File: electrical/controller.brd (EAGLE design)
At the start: 101.6 x 25.4 mm, 38 parts, among them IC1 555, Q1 IRLIB9343PBF-ND, Q3 600mA/40V, U1 POLOLU_D24V22F5, U3 MCP4725, U4 MCP4725, U5 MCP6142

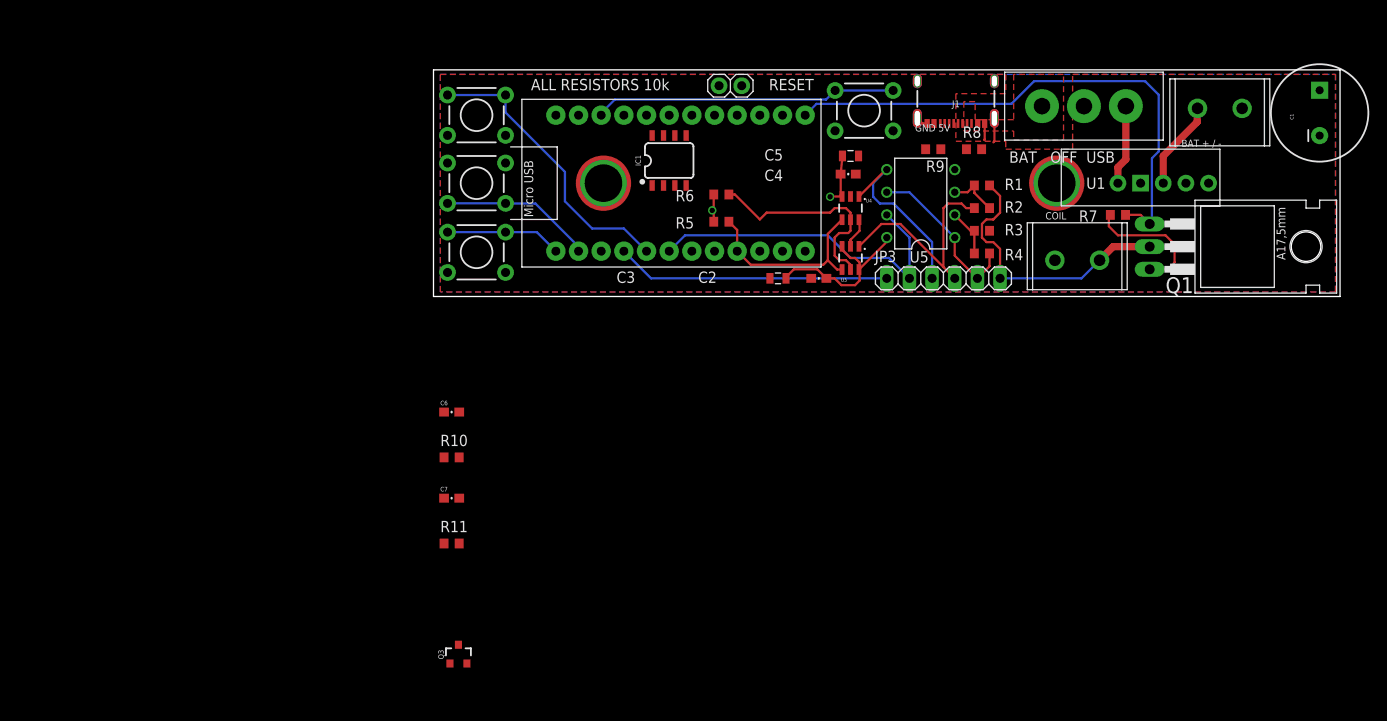
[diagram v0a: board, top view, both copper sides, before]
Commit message: Finish rev D1
Most of hte new features, except without overhauling the power system
b/c the power system requires tests with spools, which I havent done
yet.
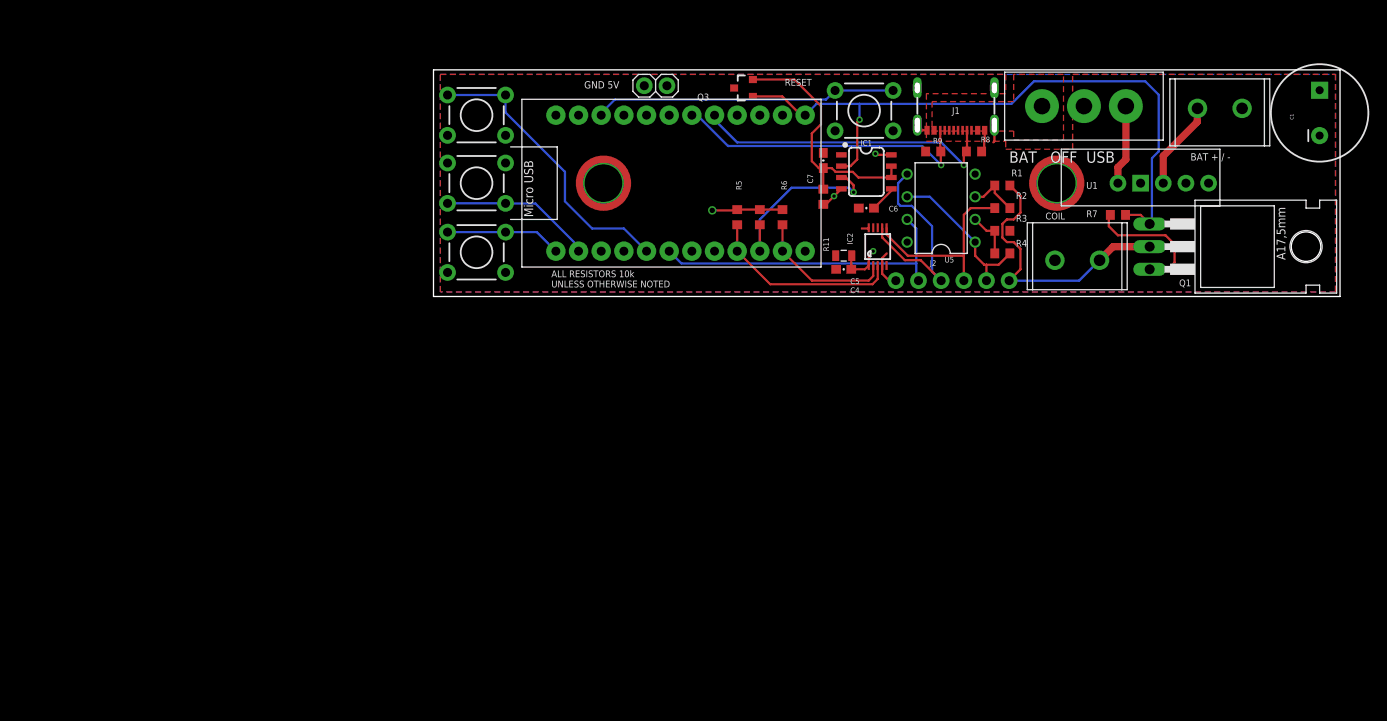
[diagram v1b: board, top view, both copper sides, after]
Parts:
- removed C2: .1uF, pie:0603-CAP
- removed C3: 10uF, pie:0805
- removed JP3: (no value), pinhead:1X06
- removed U3, U4: MCP4725, SparkFun-AnalogIC:SOT23-6
- added IC2: MCP4728, BEST_Custom:MSOP10
- added J2: (no value), SparkFun-Connectors:1X06_NO_SILK
- moved Q3 71.1 mm to (34.8, 23.4), turned to 90 degrees
- moved R11 57.0 mm to (43.7, 11.2), turned to 270 degrees
- moved C7 56.3 mm to (43.7, 15.2), turned to 270 degrees
- moved C6 51.8 mm to (48.5, 9.91), turned to 180 degrees
- moved R10 43.8 mm to (36.6, 8.89), turned to 270 degrees
- moved IC1 22.1 mm to (48.5, 14.0), turned to 270 degrees
- moved C5 11.2 mm to (46.0, 4.57), turned to 180 degrees
- moved C4 10.7 mm to (46.0, 3.05), turned to 180 degrees
- moved JP2 8.38 mm to (24.9, 23.6)
- moved R6 7.31 mm to (39.1, 8.89), turned to 90 degrees
- moved U5 2.34 mm to (56.9, 9.91)
- moved R1 2.29 mm to (63.8, 12.4)
- moved R2 2.29 mm to (63.8, 9.91)
- moved R3 2.29 mm to (63.8, 7.37)
- moved R4 2.29 mm to (63.8, 4.83)
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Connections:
- net 5V: now also IC2.1; no longer C2.1, C3.1, U3.3, U3.6, U4.3
- net COIL: now also J2.6; no longer JP3.6
- net GND: now also IC2.10, IC2.4, J2.1; no longer C2.2, C3.2, JP3.1, U3.2, U4.2, U4.6
- net INT: now also J2.2; no longer JP3.2
- net SCL: now also IC2.2; no longer U3.5, U4.5
- net SDA: now also IC2.3; no longer U3.4, U4.4
- net SHIFT: now also J2.5; no longer JP3.5
- net V1: now also IC2.6, J2.4; no longer JP3.4, U3.1
- net V2: now also IC2.7, J2.3; no longer JP3.3, U4.1
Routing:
- net CC1: track 0.00 -> 34.6 mm, vias 0 -> 1
- net CC2: track 0.00 -> 34.2 mm, vias 0 -> 1
- net GND: track 40.1 -> 11.0 mm
- net N$7: track 0.00 -> 28.8 mm
- net AUTO_RESTART: track 0.00 -> 21.2 mm, vias 0 -> 1
- net DRIVE: track 59.9 -> 75.0 mm, vias 0 -> 1
- net 5V: track 43.6 -> 32.7 mm, vias 2 -> 4
- net SCL: track 24.4 -> 15.9 mm
- net V2: track 20.8 -> 24.8 mm
- net V1: track 24.8 -> 21.5 mm
- net N$6: track 0.00 -> 2.97 mm
- net INT: track 37.8 -> 35.6 mm
- net SHIFT: track 18.7 -> 17.9 mm
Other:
- board text added: "ALL RESISTORS 10k UNLESS OTHERWISE NOTED"
- board text added: "Douglas Hutchings Double Pendulum Driver Rev D1"
- board text added: "NOTE: IF USING OSHPARK: In the DRC, set "elongation in the shapes tab To 150% This will ensure that the slots come out correctly!!"
- board text removed: "ALL RESISTORS 10k"
- board text removed: "Douglas Hutchings Double Pendulum Driver Rev C"

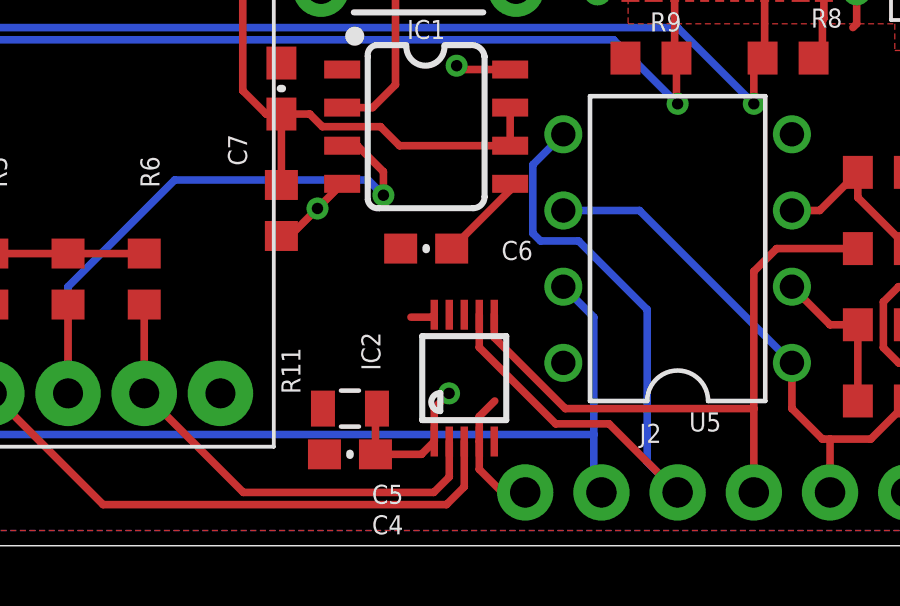
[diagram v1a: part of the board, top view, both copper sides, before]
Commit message: Create 3d model of PCB from Eagle
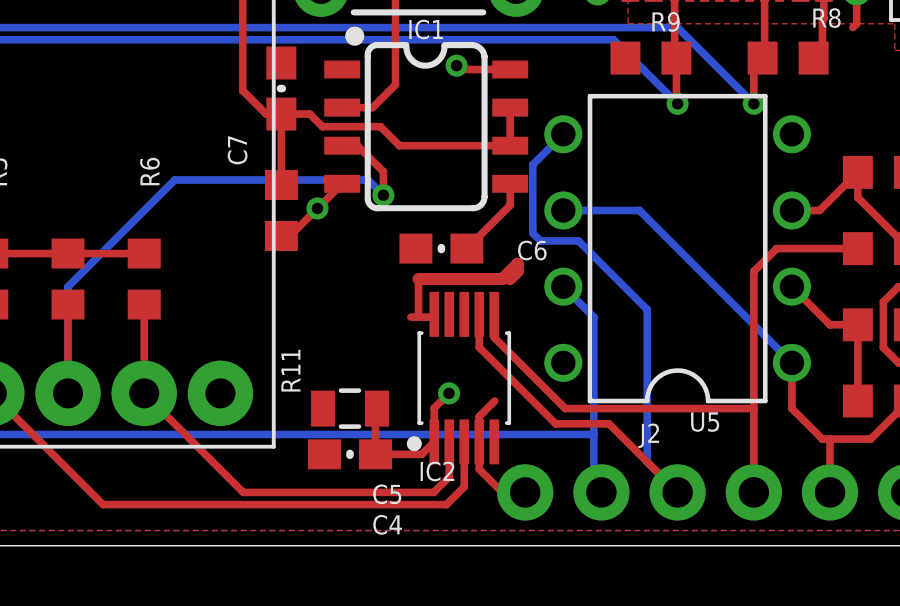
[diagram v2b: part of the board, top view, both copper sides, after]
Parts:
- IC2: device BEST_Custom:MSOP10 -> BEST_Custom:SOP50P495X110-10N
- J1: device SparkFun-Connectors:USB-C-16P-2LAYER-PADS -> BEST_Custom:USB-C-16P-2LAYER-PADS
- Q1: device transistor-fet:TO220 -> BEST_Custom:TO220
- S1, S2, S3, S4: device pie:TACTILE-PTH -> BEST_Custom:TACTILE-PTH
- ST1, ST2: device pie:2PIN_SCREW -> BEST_Custom:2PIN_SCREW
- S_PWR: device custom_parts:E-SWITCH-SPDT -> BEST_Custom:E-SWITCH-SPDT
- U1: device custom_parts:POLOLU_D24V22F5 -> BEST_Custom:POLOLU_D24V22F5
- UC1: device pie:ARDUINO_PRO_MICRO -> BEST_Custom:ARDUINO_PRO_MICRO_2D
- moved C6 0.51 mm to (49.0, 9.91)
- turned IC2 to 90 degrees
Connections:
- removed net N$1: U1.4
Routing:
- net GND: track 11.0 -> 16.4 mm

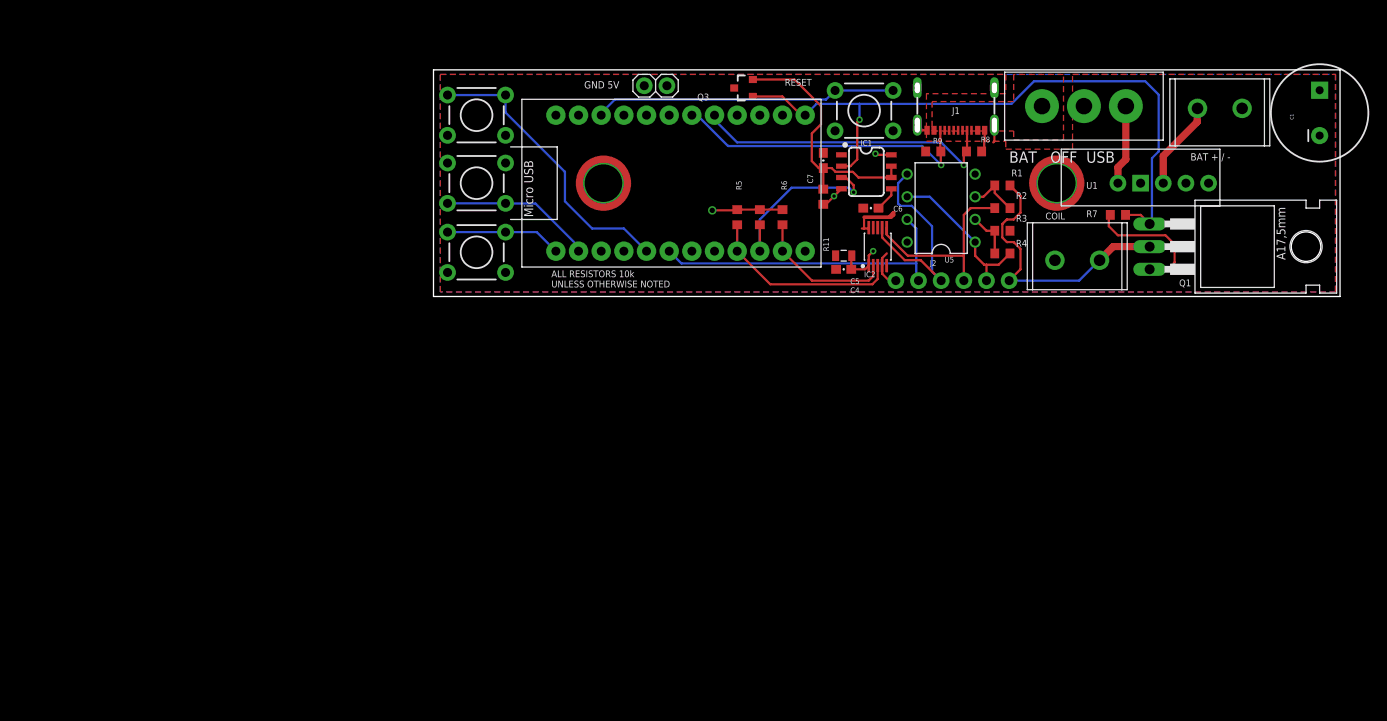
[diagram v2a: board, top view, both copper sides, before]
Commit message: some but not all of the changes for Rev D2
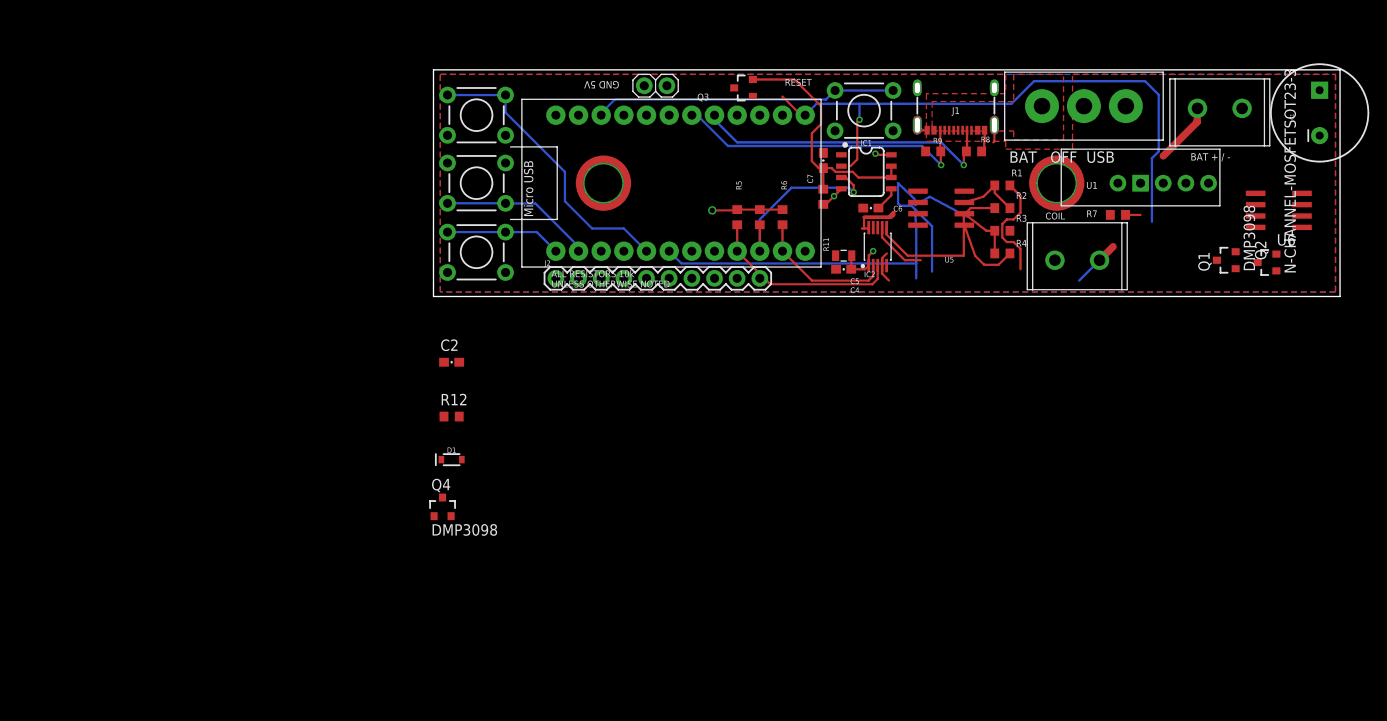
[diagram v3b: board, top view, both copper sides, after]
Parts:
- added C2: .1uF, pie:0603-CAP
- added D1: 250mA/100V, SparkFun-DiscreteSemi:SOD-323
- added Q2: N-CHANNEL-MOSFETSOT23-3, BEST_Custom:SOT23-3
- added Q4: DMP3098, BEST_Custom:SOT23-3
- added R12: 22k, pie:R0603
- added U6: MCP6042, linear:SO08
- J2: device SparkFun-Connectors:1X06_NO_SILK -> SparkFun-Connectors:1X10
- Q1: value IRLIB9343PBF-ND -> DMP3098; device BEST_Custom:TO220 -> BEST_Custom:SOT23-3
- R10, R7: value 10K -> 1M
- U5: value MCP6142 -> MCP6042; device linear:DIL08 -> linear:SO08
- UC1: device BEST_Custom:ARDUINO_PRO_MICRO_2D -> BEST_Custom:ARDUINO_PRO_MICRO
- moved J2 38.1 mm to (13.7, 2.03)
- moved Q1 2.75 mm to (88.9, 4.06), turned to 90 degrees
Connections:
- net N$2 renamed VUSB
- new net !DRIVE: IC1.2, Q3.1, UC1.16
- new net 12V: Q1.2, R7.2
- new net N$1: C2.1, D1.A, Q4.3, U6.2, U6.5
- new net N$2: R12.1, U6.1
- new net PEAK: J2.5, U6.6, U6.7
- new net PEAK_RST: J2.4, Q4.1, UC1.14
- new net VIN: C1.+, JP2.1, S_PWR.P2
- net 5V: now also Q4.2, U6.8; no longer C1.+, JP2.1, Q1.3, R7.2, S_PWR.P2
- net AUTO_RESTART: now also J2.3
- net COIL: now also J2.10, Q1.3; no longer J2.6, Q1.2
- net DRIVE: now also J2.2, Q2.1, Q2.3; no longer IC1.2, Q3.1
- net GND: now also C2.2, Q2.2, U6.4
- net INT: now also J2.6; no longer J2.2
- net N$3: now also D1.C, R12.2; no longer S_PWR.P1, U1.1
- net SHIFT: now also J2.9, U6.3; no longer J2.5
- net V1: now also J2.8; no longer J2.4
- net V2: now also J2.7; no longer J2.3
- net VBAT: now also S_PWR.P1; no longer U1.3
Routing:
- net 5V: track 32.7 -> 18.0 mm
- net COIL: track 31.6 -> 17.9 mm
- net N$3: track 9.00 -> 0.00 mm
- net DRIVE: track 75.0 -> 68.9 mm
- net V2: track 24.8 -> 21.3 mm
- net VBAT: track 9.97 -> 6.93 mm
- net V1: track 21.6 -> 18.8 mm
- net SHIFT: track 17.9 -> 15.1 mm
- net N$5: track 5.26 -> 6.60 mm
- net N$4: track 5.97 -> 7.27 mm
- net GND: track 16.4 -> 15.6 mm

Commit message: Most, but not all, of rev D2
Still need to test CC1 / CC2.
Add debug pinout silkscreen labels.
See if we can still use resistor arrays.
Calculate new values for the trigger op-amp network.
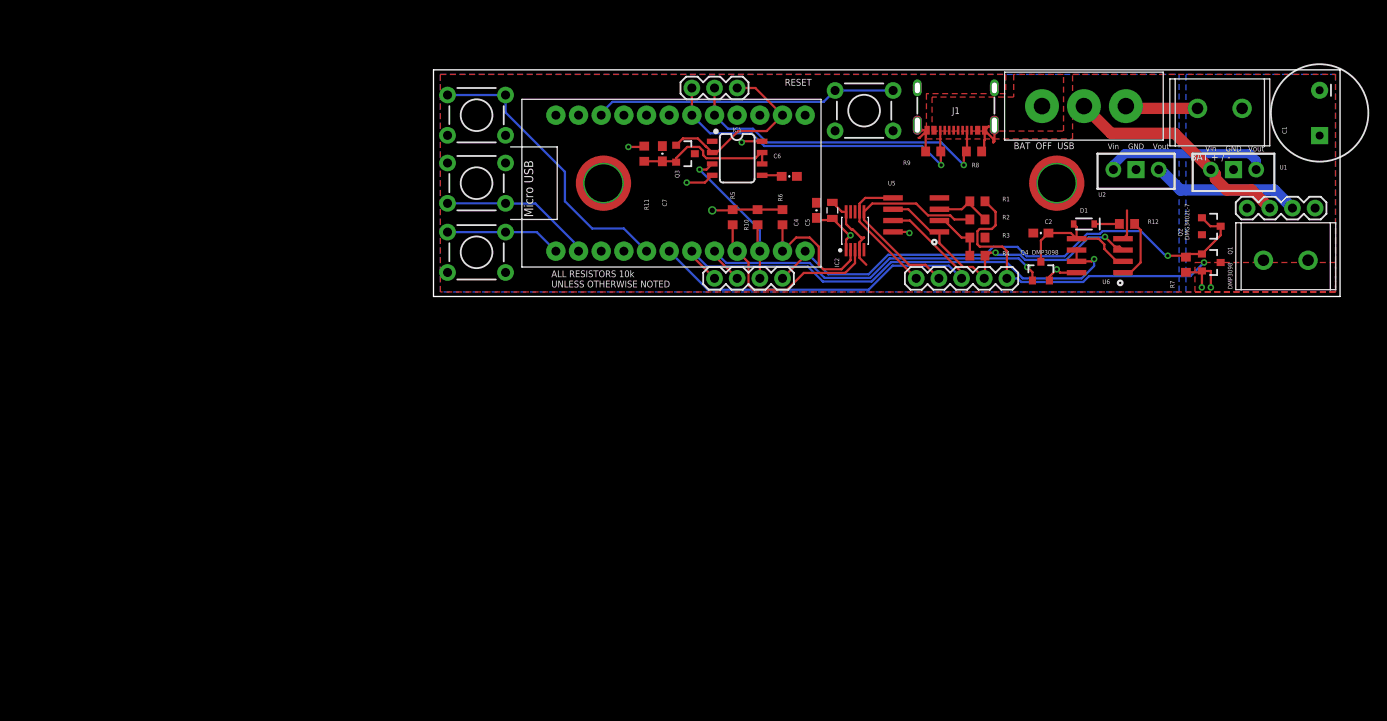
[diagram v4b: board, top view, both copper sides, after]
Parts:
- removed JP2: (no value), pie:1X02
- added J3: 455-1750-1-ND, SparkFun-Connectors:1X03
- added J4: (no value), SparkFun-Connectors:1X05
- added J5: (no value), SparkFun-Connectors:1X04
- added U2: U3V16F15, BEST_Custom:POLOLU_VOLTAG_REGULATOR_D45V1E1FX_VERT
- J2: device SparkFun-Connectors:1X10 -> SparkFun-Connectors:1X04
- Q2: value N-CHANNEL-MOSFETSOT23-3 -> DMG3402L-7
- U1: value POLOLU_D24V22F5 -> U3V16F15; device BEST_Custom:POLOLU_D24V22F5 -> BEST_Custom:POLOLU_VOLTAG_REGULATOR_U3V16FX_VERT
- UC1: value ARDUINO_PRO_MICRO -> (none); device BEST_Custom:ARDUINO_PRO_MICRO -> BEST_Custom:ARDUINO_PRO_MICRO_2D
- moved R12 78.7 mm to (77.7, 8.13), turned to 180 degrees
- moved J2 77.9 mm to (91.2, 9.91)
- moved D1 75.6 mm to (72.9, 8.13), turned to 180 degrees
- moved Q4 72.1 mm to (68.1, 2.79)
- moved C2 67.6 mm to (68.1, 7.11), turned to 180 degrees
- moved ST2 23.4 mm to (89.9, 0.76)
- moved U6 20.7 mm to (74.7, 4.57)
- moved R11 20.6 mm to (23.6, 16.0), turned to 90 degrees
- moved C7 18.1 mm to (25.7, 16.0)
- moved IC1 14.6 mm to (34.0, 15.5)
- moved Q3 9.89 mm to (28.2, 16.0), turned to 270 degrees
- moved C6 9.81 mm to (39.9, 13.5), turned to 0 degrees
- moved U1 9.56 mm to (89.7, 14.2)
- moved R7 9.45 mm to (84.3, 3.56), turned to 270 degrees
- moved Q2 7.54 mm to (87.1, 7.87), turned to 270 degrees
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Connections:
- removed net 12V: Q1.2, R7.2
- removed net PEAK: J2.5, U6.6, U6.7
- new net 15V: C1.+, J2.4, Q1.2, R7.2, U1.VOUT, U2.VIN
- new net A_PEAK: J5.4, U6.6, U6.7, UC1.4
- net !DRIVE: now also J3.1
- net 5V: now also J2.3, U2.VOUT
- net AUTO_RESTART: now also J5.2; no longer J2.3
- net CC1: now also J3.2
- net CC2: now also J3.3
- net COIL: now also J4.5; no longer J2.10
- net DRIVE: now also J5.1, UC1.9; no longer J2.2, UC1.10
- net GND: now also U1.GND, U2.GND; no longer JP2.2, U1.2
- net INT: now also J4.3; no longer J2.6
- net PEAK_RST: now also J5.3, UC1.5; no longer J2.4, UC1.14
- net SHIFT: now also J4.4; no longer J2.9
- net V1: now also J4.2; no longer J2.8
- net V2: now also J4.1; no longer J2.7
- net VIN: now also J2.2, U1.VIN; no longer C1.+, JP2.1
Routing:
- net A_PEAK: track 0.00 -> 57.2 mm, vias 0 -> 1
- net PEAK_RST: track 0.00 -> 43.4 mm, vias 0 -> 1
- net 5V: track 18.0 -> 44.5 mm, vias 4 -> 7
- net VIN: track 0.00 -> 25.9 mm
- net 15V: track 0.00 -> 25.0 mm, vias 0 -> 2
- net !DRIVE: track 0.00 -> 21.0 mm
- net SHIFT: track 15.1 -> 34.4 mm, vias 0 -> 2
- net COIL: track 17.9 -> 36.8 mm, vias 0 -> 1
- net N$1: track 0.00 -> 15.3 mm
- net N$7: track 28.8 -> 16.7 mm
- net INT: track 35.8 -> 47.0 mm
- net GND: track 15.6 -> 25.6 mm
- net DRIVE: track 68.9 -> 60.6 mm
- net N$2: track 0.00 -> 7.04 mm
- net V2: track 21.3 -> 15.0 mm
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- added copper zone on layer 16, net 15V
- added copper zone on layer 1, net COIL
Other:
- board text added: "Douglas Hutchings Double Pendulum Driver Rev D2"
- board text removed: "COIL"
- board text removed: "Douglas Hutchings Double Pendulum Driver Rev D1"
- board text removed: "GND 5V"
